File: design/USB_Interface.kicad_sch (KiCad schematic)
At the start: 7 parts, among them J9 USB_C_Receptacle_USB2.0_16P

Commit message: Pequeños cambios
Pequeños cambios en esquemático
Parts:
- renumbered R36 to R37, R37 to R38, R38 to R39, R39 to R40, R40 to R41, R41 to R42
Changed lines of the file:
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@@
 		(on_board yes)
 		(dnp no)
-		(property "Reference" "R39"
+		(property "Reference" "R40"
 			(at 133.096 97.536 90)
 			(effects
@@
 			(project "ESCX"
 				(path "/6389d757-a1bd-4c0a-9d55-6114b19cc67a/3b58b0da-7904-4d95-a506-9abfc64a393e"
-					(reference "R39")
+					(reference "R40")
 					(unit 1)
 				)
@@
 		(on_board yes)
 		(dnp no)
-		(property "Reference" "R41"
+		(property "Reference" "R42"
 			(at 163.83 106.68 0)
 			(effects
@@
 			(project "ESCX"
 				(path "/6389d757-a1bd-4c0a-9d55-6114b19cc67a/3b58b0da-7904-4d95-a506-9abfc64a393e"
-					(reference "R41")
+					(reference "R42")
 					(unit 1)
 				)
@@
 		(dnp no)
 		(fields_autoplaced yes)
-		(property "Reference" "#PWR069"
+		(property "Reference" "#PWR071"
 			(at 85.09 130.81 0)
 			(effects
@@
 			(project "ESCX"
 				(path "/6389d757-a1bd-4c0a-9d55-6114b19cc67a/3b58b0da-7904-4d95-a506-9abfc64a393e"
-					(reference "#PWR069")
+					(reference "#PWR071")
 					(unit 1)
 				)
@@
 		(dnp no)
 		(fields_autoplaced yes)
-		(property "Reference" "#PWR071"
+		(property "Reference" "#PWR073"
 			(at 128.27 81.28 0)
 			(effects
@@
 			(project "ESCX"
 				(path "/6389d757-a1bd-4c0a-9d55-6114b19cc67a/3b58b0da-7904-4d95-a506-9abfc64a393e"
-					(reference "#PWR071")
+					(reference "#PWR073")
 					(unit 1)
 				)
@@
 		(dnp no)
 		(fields_autoplaced yes)
-		(property "Reference" "#PWR073"
+		(property "Reference" "#PWR075"
 			(at 167.64 124.46 0)
 			(effects
@@
 			(project "ESCX"
 				(path "/6389d757-a1bd-4c0a-9d55-6114b19cc67a/3b58b0da-7904-4d95-a506-9abfc64a393e"
-					(reference "#PWR073")
+					(reference "#PWR075")
 					(unit 1)
 				)
@@
 		(dnp no)
 		(fields_autoplaced yes)
-		(property "Reference" "R36"
+		(property "Reference" "R37"
 			(at 111.76 74.93 90)
 			(effects
@@
 			(project "ESCX"
 				(path "/6389d757-a1bd-4c0a-9d55-6114b19cc67a/3b58b0da-7904-4d95-a506-9abfc64a393e"
-					(reference "R36")
+					(reference "R37")
 					(unit 1)
 				)
@@
 		(dnp no)
 		(fields_autoplaced yes)
-		(property "Reference" "#PWR070"
+		(property "Reference" "#PWR072"
 			(at 118.11 81.28 0)
 			(effects
@@
 			(project "ESCX"
 				(path "/6389d757-a1bd-4c0a-9d55-6114b19cc67a/3b58b0da-7904-4d95-a506-9abfc64a393e"
-					(reference "#PWR070")
+					(reference "#PWR072")
 					(unit 1)
 				)
@@
 		(dnp no)
 		(fields_autoplaced yes)
-		(property "Reference" "#PWR072"
+		(property "Reference" "#PWR074"
 			(at 157.48 127 0)
 			(effects
@@
 			(project "ESCX"
 				(path "/6389d757-a1bd-4c0a-9d55-6114b19cc67a/3b58b0da-7904-4d95-a506-9abfc64a393e"
-					(reference "#PWR072")
+					(reference "#PWR074")
 					(unit 1)
 				)
@@
 		(on_board yes)
 		(dnp no)
-		(property "Reference" "R38"
+		(property "Reference" "R39"
 			(at 132.588 92.202 90)
 			(effects
@@
 			(project "ESCX"
 				(path "/6389d757-a1bd-4c0a-9d55-6114b19cc67a/3b58b0da-7904-4d95-a506-9abfc64a393e"
-					(reference "R38")
+					(reference "R39")
 					(unit 1)
 				)
@@
 		(on_board yes)
 		(dnp no)
-		(property "Reference" "R40"
+		(property "Reference" "R41"
 			(at 153.67 106.68 0)
 			(effects
@@
 			(project "ESCX"
 				(path "/6389d757-a1bd-4c0a-9d55-6114b19cc67a/3b58b0da-7904-4d95-a506-9abfc64a393e"
-					(reference "R40")
+					(reference "R41")
 					(unit 1)
 				)
@@
 		(on_board yes)
 		(dnp no)
-		(property "Reference" "R37"
+		(property "Reference" "R38"
 			(at 116.332 103.886 90)
 			(effects
@@
 			(project "ESCX"
 				(path "/6389d757-a1bd-4c0a-9d55-6114b19cc67a/3b58b0da-7904-4d95-a506-9abfc64a393e"
-					(reference "R37")
+					(reference "R38")
 					(unit 1)
 				)

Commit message: Agrego MFR# de conectores
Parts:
- J9: Manufacturer (none) -> Global Connector Technology; Manufacturer Product Number  (none) -> USB4105-GF-A
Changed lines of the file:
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@@
+			)
+		)
+		(property "Manufacturer" "Global Connector Technology"
+			(at 92.71 96.52 0)
+			(effects
+				(font
+					(size 1.27 1.27)
+				)
+				(hide yes)
+			)
+		)
+		(property "Manufacturer Product Number " "USB4105-GF-A"
+			(at 92.71 96.52 0)
+			(effects
+				(font
+					(size 1.27 1.27)
+				)
+				(hide yes)
 			)
 		)

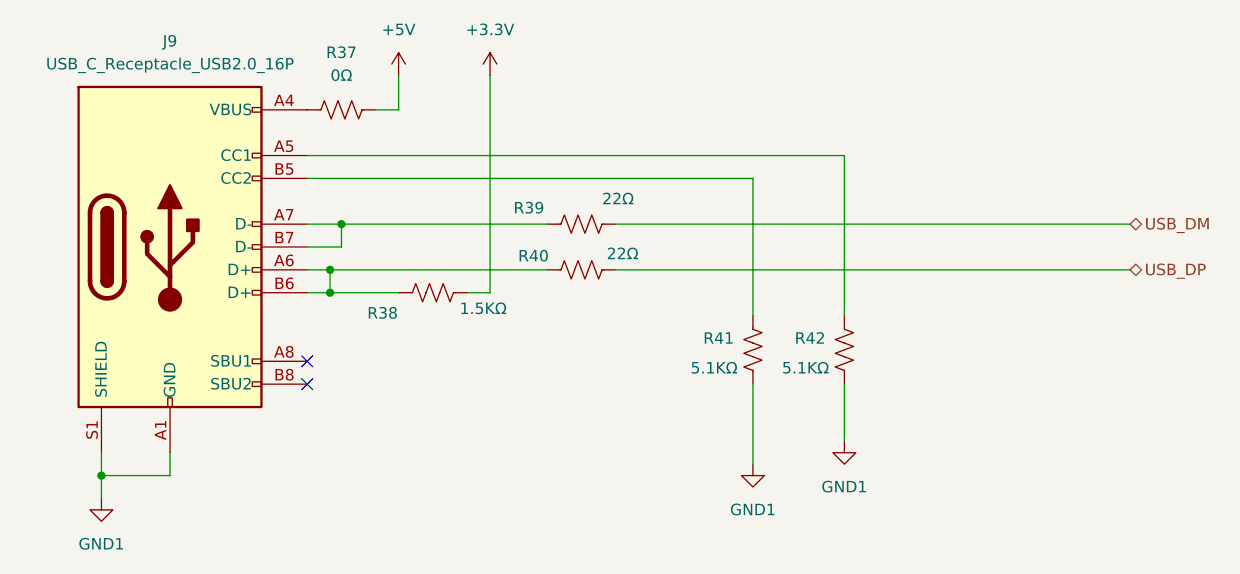
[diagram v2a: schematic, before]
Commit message: Arreglos y cambios
Cambios en ruteos, dimensión de la placa, tamaño de las vías, parámetros de diseño jlcpb (constraints). Agregado de pad térmico de transistores, duplicado de capa inferior y superior para mejor disipación.
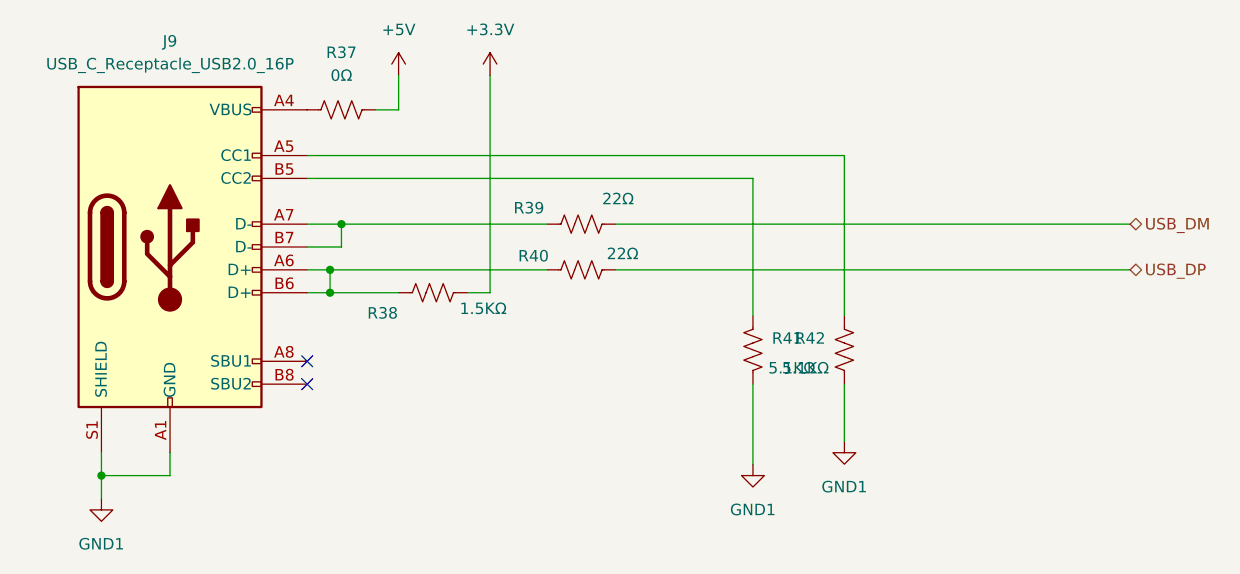
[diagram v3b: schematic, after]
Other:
- moved on the sheet: R41
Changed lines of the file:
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@@
 	(symbol
 		(lib_id "Device:R_US")
-		(at 157.48 107.95 180)
+		(at 157.48 107.95 0)
+		(mirror x)
 		(unit 1)
 		(exclude_from_sim no)
@@
 		(dnp no)
 		(property "Reference" "R41"
-			(at 153.67 106.68 0)
+			(at 161.29 106.68 0)
 			(effects
 				(font
@@
 		)
 		(property "Value" "5.1KΩ"
-			(at 153.162 109.982 0)
+			(at 161.798 109.982 0)
 			(effects
 				(font
@@
 		)
 		(property "Footprint" "Resistor_SMD:R_0603_1608Metric"
-			(at 156.464 107.696 90)
+			(at 158.496 107.696 90)
 			(effects
 				(font

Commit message: Rotado del driver
Rotado del driver, cambiado de capacitores, disipación de transistores, cambiado de capacitores de semi puentes.
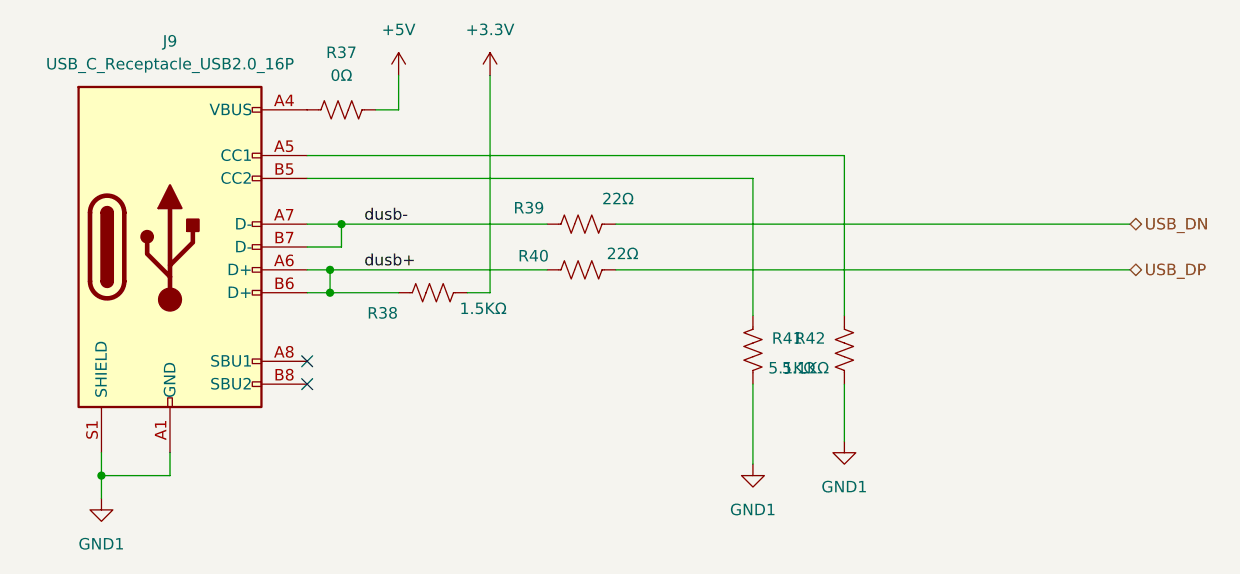
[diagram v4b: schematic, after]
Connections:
- net dusb+: now reaches J9.A6 (D+), J9.B6 (D+), R38.2, R40.2
- net dusb-: now reaches J9.A7 (D-), J9.B7 (D-), R39.2
- net USB_DM renamed USB_DN
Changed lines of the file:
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@@
+		)
+	)
+	(label "dusb-"
+		(at 114.3 93.98 0)
+		(fields_autoplaced yes)
+		(effects
+			(font
+				(size 1.27 1.27)
+			)
+			(justify left bottom)
+		)
+	)
+	(label "dusb+"
+		(at 114.3 99.06 0)
+		(fields_autoplaced yes)
+		(effects
+			(font
+				(size 1.27 1.27)
+			)
+			(justify left bottom)
 		)
 	)
@@
 		)
 	)
-	(hierarchical_label "USB_DM"
+	(hierarchical_label "USB_DN"
 		(shape bidirectional)
 		(at 199.39 93.98 0)
